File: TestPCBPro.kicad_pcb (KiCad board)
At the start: 2 copper layers, 100 x 50 mm, 82 parts, among them J1 Analog, J10 J3011G21DNL, J2 Digital, J3 CANBUS, J4 UART, J5 SPI, J6 I2C, J7 Power, J8 10118192-0001LF, J9 ICSP, SW1 Reset Button, U1 PIC32MX775F256L-80I/PT, U2 AZ1117EH-3.3TRG1, U3 LFSPXO025560REEL, U4 LAN8740A-EN, Y1 Crystal

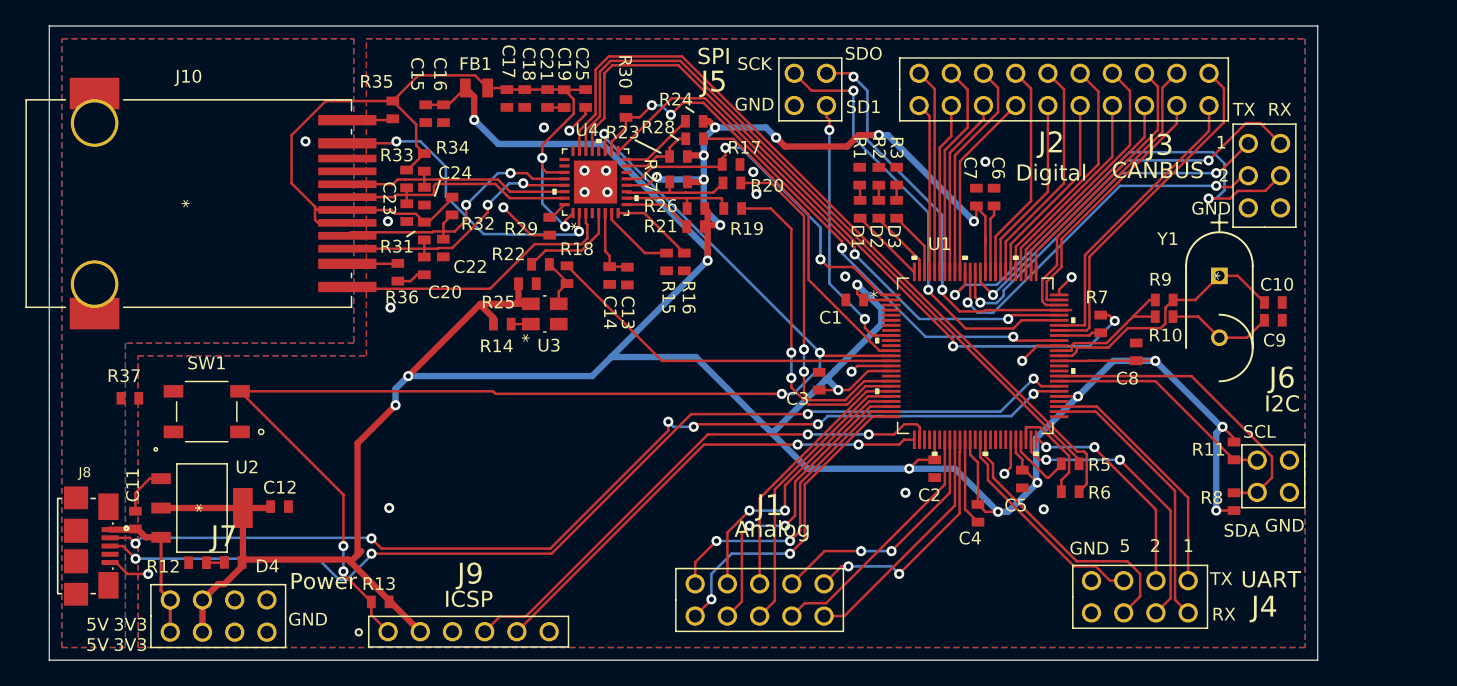
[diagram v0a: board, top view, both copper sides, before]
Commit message: Imported AISLER 2Layer-Complex design rules Added Silkscreen to all passives to help with orientation Moved C15 and C16 to the back in order to be physically closer to the VDDIO pin of the LAN8740a Increased trace width of some 5v traces to the proper 0.5mm
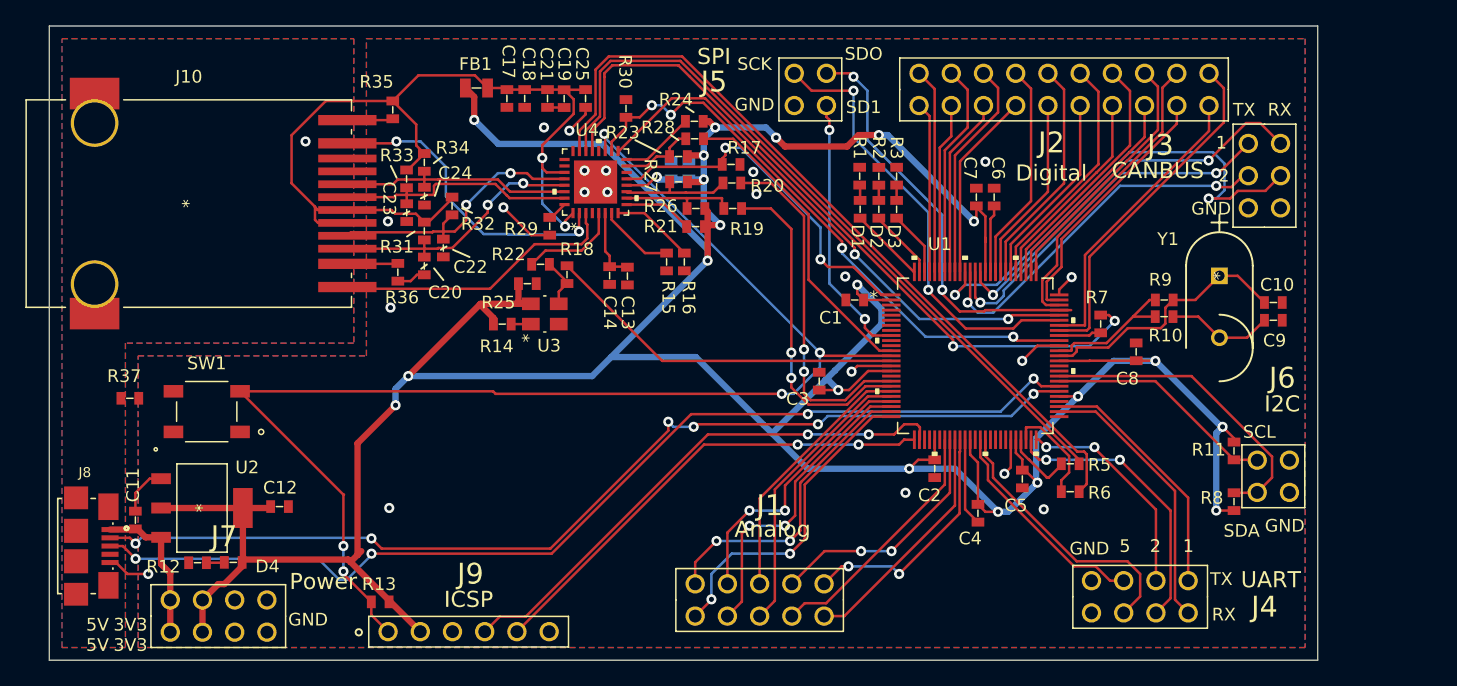
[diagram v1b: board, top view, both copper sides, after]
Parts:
- C14, C17, C21: value 1.0u -> 1u
- C15: value 1.0u -> 1u; moved to B.Cu
- C16: moved to B.Cu
- moved C15 21.8 mm to (132.8, 89.5), turned to 90 degrees
- moved C16 19.2 mm to (131.4, 89.5), turned to 90 degrees
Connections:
- net Net-(C13-Pad1) renamed /Ethernet/VDDCR
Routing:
- net +3V3: track 305.8 -> 302.2 mm

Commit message: Fixed nINT not actually being connected to 3v3 Changed the pic32MX7* 100 pin footprint from the T package to the F package Added some silkscreen around the DIGITAL and ANALOG headers
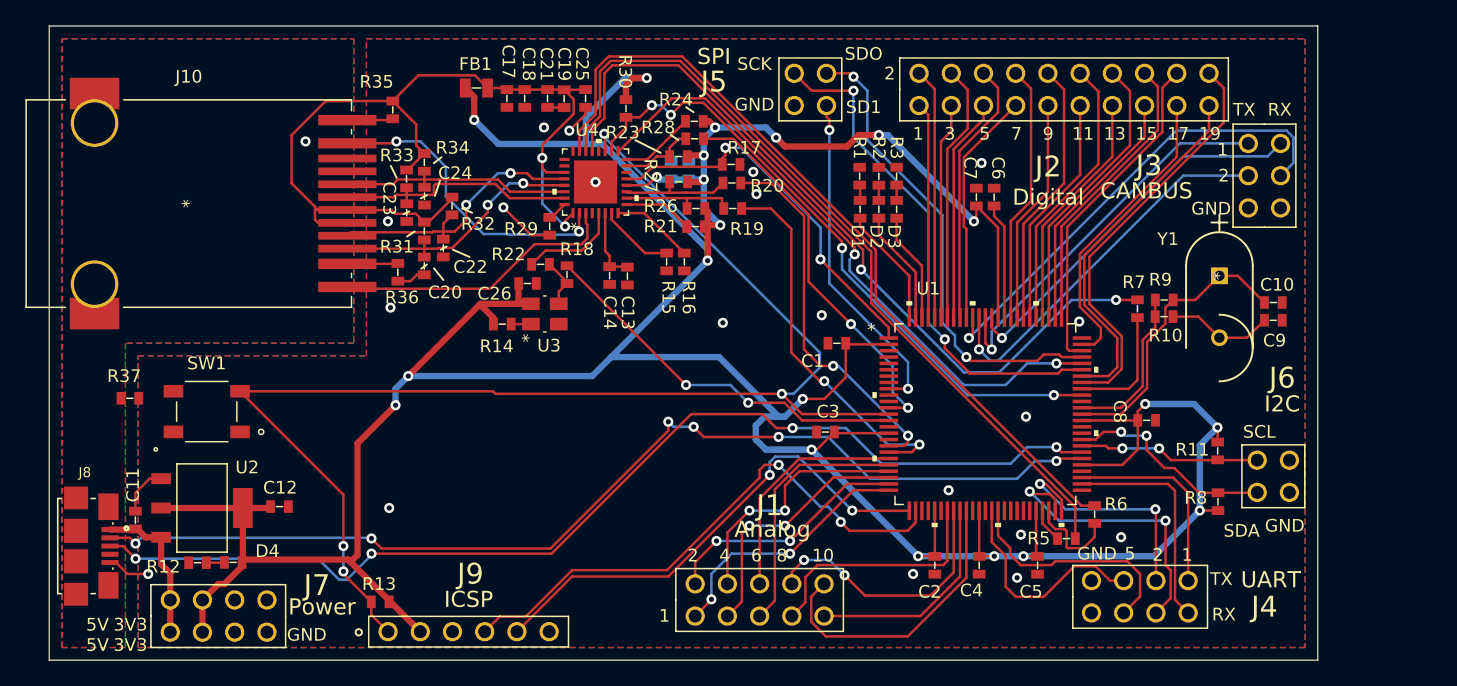
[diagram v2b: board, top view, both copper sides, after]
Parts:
- removed R25: 0.01u, Lambley:0603-1608M
- added C26: .01u, Lambley:0603-1608M, F.Cu at (119.5, 97.9)
- R15, R16, R17, R23, R26, R27: value 4.7K -> 4.7k
- U1: footprint ul_PIC32MX775F256L-80I-PT:PIC32MX775F256L-80I&slash_PT -> ul_PIC32MX764F128L-I-PF:PIC32MX764F128L-I&slash_PF
- moved C2 7.61 mm to (152.2, 118.4)
- moved C5 6.91 mm to (160.3, 118.4)
- moved R5 5.91 mm to (164.3, 116.8)
- moved C8 4.94 mm to (168.4, 108.7), turned to 0 degrees
- moved U1 4.67 mm to (156.8, 107.6)
- moved C4 4.10 mm to (155.7, 118.4)
- moved C1 3.69 mm to (146.2, 101.4)
- moved R7 3.14 mm to (169.4, 100.4)
- moved C3 2.49 mm to (145.3, 108.4), turned to 180 degrees
- moved R11 1.29 mm to (174.5, 109.3)
- moved R8 1.26 mm to (175.7, 115.7)
- moved R6 1.26 mm to (164.8, 114.4), turned to -90 degrees
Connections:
- R30 pad 1: +3.3V -> +3V3
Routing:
- net GND: track 36.2 -> 17.8 mm, vias 21 -> 20
- net +3V3: track 302.2 -> 314.5 mm
- net SDA2: track 24.6 -> 16.7 mm, vias 0 -> 2
- net Net-(R7-Pad1): track 3.36 -> 9.58 mm
- net /Ethernet/CRS_DV: track 24.8 -> 30.8 mm, vias 0 -> 2
- net /Ethernet/MDC: track 44.1 -> 50.0 mm
- net /Ethernet/TXD0: track 58.2 -> 64.0 mm
- net 69: track 23.4 -> 28.8 mm
- net 68: track 27.4 -> 32.8 mm
- net SDI1: track 21.1 -> 26.5 mm
- net AN0: track 25.7 -> 20.6 mm
- net AN1: track 24.6 -> 19.5 mm
- net SCK1: track 35.3 -> 40.3 mm
- net SDO1: track 33.0 -> 37.6 mm
- net /Ethernet/nINT: track 46.7 -> 51.0 mm
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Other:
- board text added: "10"
- board text added: "11"
- board text added: "13"
- board text added: "15"
- board text added: "17"
- board text added: "19"
- board text added: "3"
- board text added: "4"
- board text added: "6"
- board text added: "7"
- board text added: "8"
- board text added: "9"

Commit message: Added connection for MDIO to the PIC Complete redesign of board, reduced size from 100x50 to 75x35mm Readded C15 and C16 to the front Added some test points
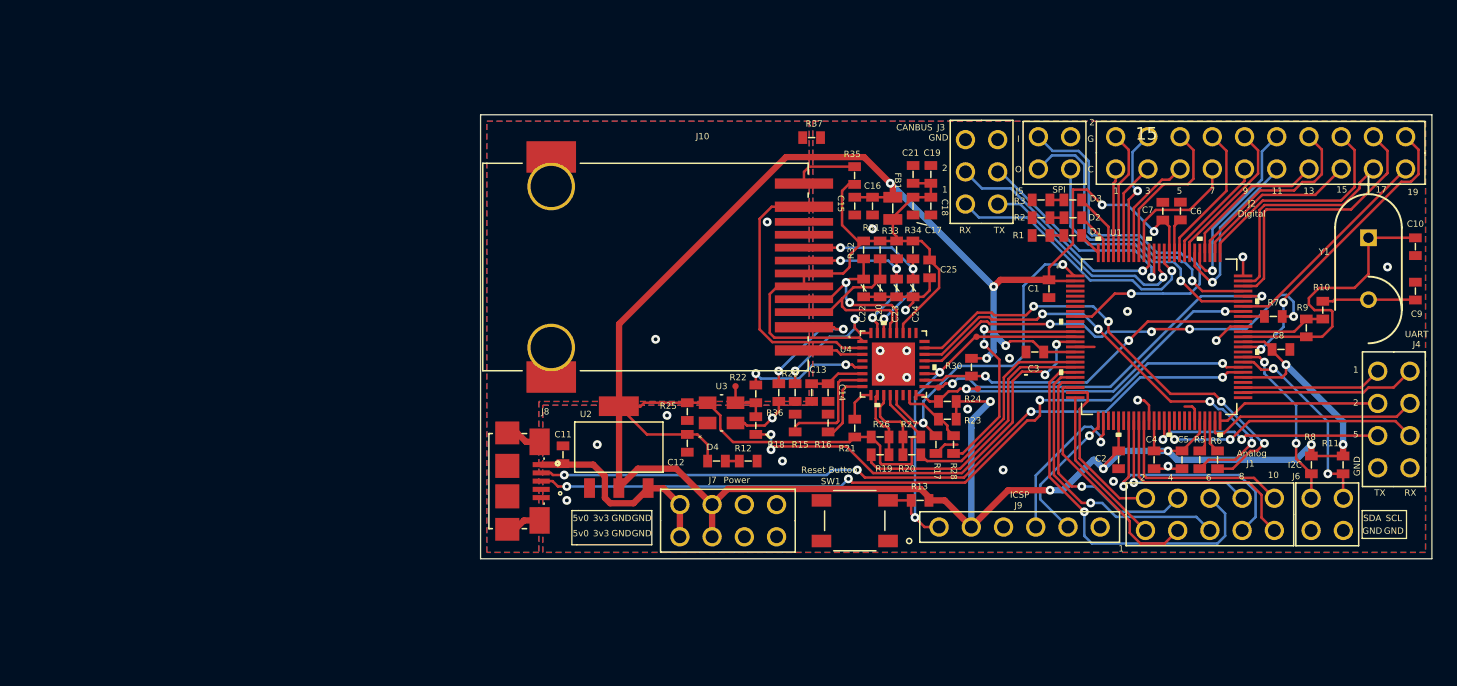
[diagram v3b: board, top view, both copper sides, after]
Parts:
- removed C26: .01u, Lambley:0603-1608M
- removed R14: 0-DNP, Lambley:0603-1608M
- added R25: 0.01u, Lambley:0603-1608M, F.Cu at (133.9, 108.5)
- added REF: .5mm TP, Lambley:.5mm TP, F.Cu at (153.1, 105.5)
- added REF**: .5mm TP, Lambley:.5mm TP, F.Cu at (156.1, 101.5)
- added REF**: .5mm TP, Lambley:.5mm TP, F.Cu at (137.1, 105.4)
- added REF**: .5mm TP, Lambley:.5mm TP, F.Cu at (156.2, 105.6)
- C15, C16: moved to F.Cu
- R15, R16, R17, R23, R26, R27: value 4.7k -> 4.7K
- U1: footprint ul_PIC32MX764F128L-I-PF:PIC32MX764F128L-I&slash_PF -> ul_PIC32MX775F256L-80I-PT:PIC32MX775F256L-80I&slash_PT
- moved R37 57.5 mm to (144.2, 85.2)
- moved SW1 51.8 mm to (146.5, 116.0)
- moved J9 44.2 mm to (153.2, 116.5)
- moved R13 43.3 mm to (150.5, 115.0)
- moved R12 41.7 mm to (136.9, 111.9), turned to 0 degrees
- moved D4 41.4 mm to (136.8, 110.7), turned to 180 degrees
- moved J7 40.9 mm to (132.7, 114.7)
- moved C24 39.2 mm to (150.5, 96.5)
- moved R34 39.1 mm to (151.7, 95.8)
- moved C23 39.1 mm to (149.2, 96.5)
- moved R33 39.0 mm to (150.4, 95.8)
- moved R35 38.3 mm to (147.1, 89.9), turned to 90 degrees
- moved J10 36.3 mm to (130.0, 96.0)
- moved J1 36.1 mm to (169.4, 114.2)
- moved C20 36.0 mm to (147.9, 96.5)
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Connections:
- net Net-(J10-Pad2) renamed /Ethernet/LED_LINK_OUT
- J2 pad 20: 68 -> 61
- R24 pad 2: Net-(R24-Pad2) -> /Ethernet/MDIO
- U1 pad 61: unconnected-(U1-Pad61) -> 61
- U1 pad 68: 68 -> /Ethernet/MDIO
- U3 pad 1: Net-(R14-Pad1) -> unconnected-(U3-Pad1)
- U4 pad 16: Net-(R24-Pad2) -> /Ethernet/MDIO
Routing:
- net /ICSP/MCLR: track 106.4 -> 30.9 mm, vias 4 -> 2
- net +3V3: track 314.5 -> 252.6 mm, vias 21 -> 13
- net 68: track 32.8 -> 0.00 mm
- net /Ethernet/MDIO: track 0.00 -> 30.0 mm, vias 0 -> 2
- net /ICSP/PGED: track 43.2 -> 13.3 mm, vias 2 -> 1
- net /ICSP/PGEC: track 39.0 -> 11.2 mm, vias 2 -> 1
- net /Ethernet/TX_EN: track 62.3 -> 34.5 mm, vias 2 -> 4
- net /Ethernet/TXD0: track 64.0 -> 36.7 mm, vias 0 -> 4
- net /Ethernet/TXD1: track 63.7 -> 37.8 mm, vias 0 -> 4
- net /USB and Power/D-: track 84.4 -> 59.3 mm, vias 6 -> 4
- net /USB and Power/D+: track 85.5 -> 60.6 mm
- net 61: track 0.00 -> 24.3 mm, vias 0 -> 2
- net /Ethernet/nINT: track 51.0 -> 27.4 mm, vias 4 -> 2
- net VDD1A: track 71.8 -> 48.9 mm, vias 2 -> 0
- net SCK1: track 40.3 -> 21.1 mm, vias 2 -> 1
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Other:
- board size 100 x 50 mm -> 75 x 35 mm
- board text added: "*"
- board text added: "3v3"
- board text added: "5v0"
- board text added: "C"
- board text added: "G"
- board text added: "I"
- board text added: "O"
- board text removed: "3V3"
- board text removed: "5V"
- board text removed: "SCK"
- board text removed: "SD1"
- board text removed: "SDO"

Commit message: Actually changed to the PIC to the F package this time
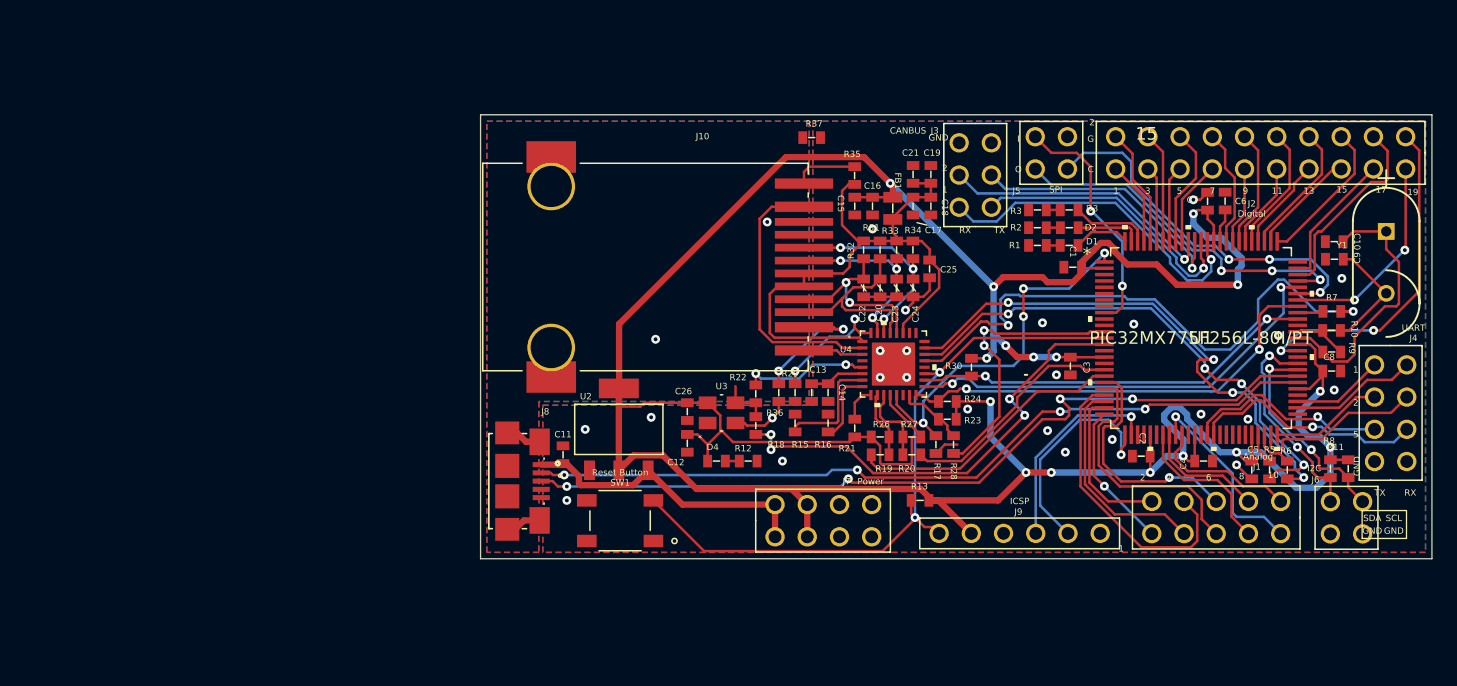
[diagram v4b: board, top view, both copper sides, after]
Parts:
- removed R25: 0.01u, Lambley:0603-1608M
- removed REF, REF** (x3): .5mm TP, Lambley:.5mm TP
- added C26: .01u, Lambley:0603-1608M, F.Cu at (132.7, 106.2)
- R15, R16, R17, R23, R26, R27: value 4.7K -> 4.7k
- U1: footprint ul_PIC32MX775F256L-80I-PT:PIC32MX775F256L-80I&slash_PT -> ul_PIC32MX764F128L-I-PF:PIC32MX764F128L-I&slash_PF
- moved SW1 18.5 mm to (128.0, 116.0)
- moved J7 7.50 mm to (140.2, 114.7)
- moved C9 7.23 mm to (185.5, 94.8), turned to 180 degrees
- moved R5 5.56 mm to (179.8, 113.2)
- moved R6 5.56 mm to (181.2, 113.2)
- moved C5 5.56 mm to (177.2, 110.8)
- moved C10 4.65 mm to (185.4, 93.4), turned to 180 degrees
- moved R7 4.63 mm to (183.0, 100.1)
- moved R9 4.48 mm to (185.2, 102.1), turned to 180 degrees
- moved C8 4.35 mm to (182.9, 104.8)
- moved C4 3.83 mm to (172.8, 111.9), turned to 0 degrees
- moved C1 3.80 mm to (164.8, 95.4), turned to 180 degrees
- moved C6 3.61 mm to (176.3, 92.0)
- moved C7 3.61 mm to (174.9, 92.0)
- moved C2 3.55 mm to (170.2, 110.3), turned to 180 degrees
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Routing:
- net /ICSP/MCLR: track 30.9 -> 54.7 mm
- net +3V3: track 252.6 -> 266.1 mm, vias 13 -> 16
- net SDI1: track 32.5 -> 19.0 mm, vias 1 -> 2
- net AN5: track 30.7 -> 19.0 mm
- net /Ethernet/TX_EN: track 34.5 -> 45.2 mm, vias 4 -> 2
- net GND: track 26.5 -> 17.5 mm, vias 21 -> 25
- net SCK1: track 21.1 -> 29.4 mm, vias 1 -> 3
- net AN8: track 20.4 -> 12.1 mm, vias 1 -> 0
- net 81: track 14.2 -> 6.73 mm, vias 1 -> 0
- net /ICSP/PGEC: track 11.2 -> 18.3 mm
- net +5V: track 16.7 -> 23.6 mm
- net 74: track 17.3 -> 10.9 mm
- net 76: track 17.6 -> 11.7 mm
- net 73: track 21.5 -> 15.6 mm
- net /Ethernet/MDIO: track 30.0 -> 35.2 mm
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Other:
- board text removed: "3v3"
- board text removed: "5v0"

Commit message: Re-added test points and fixed silkscreen
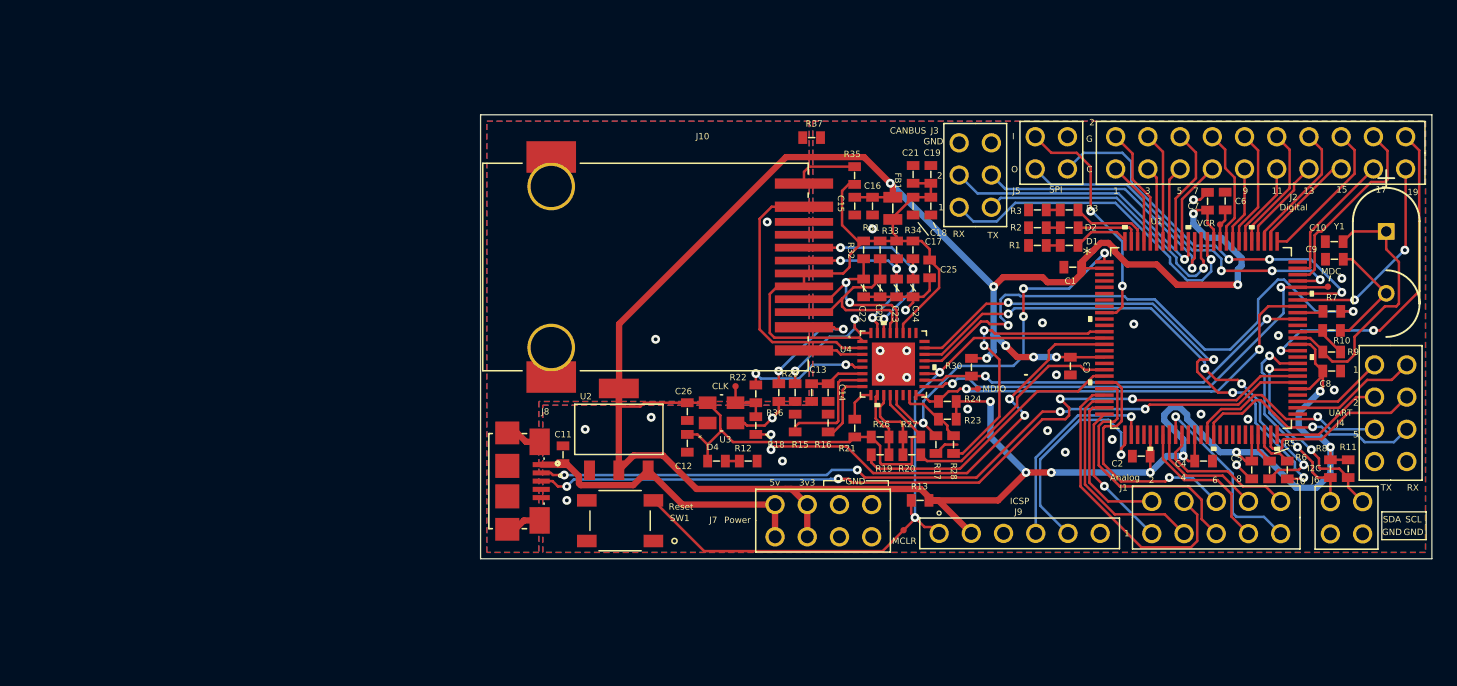
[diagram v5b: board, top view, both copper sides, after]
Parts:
- added CLK: .5mm TP, Lambley:.5mm TP, F.Cu at (137.1, 105.4)
- added MCLR: .5mm TP, Lambley:.5mm TP, F.Cu at (150.3, 116.8)
- added MDC: .5mm TP, Lambley:.5mm TP, F.Cu at (183.8, 97.5)
- added MDIO: .5mm TP, Lambley:.5mm TP, F.Cu at (156.2, 105.6)
- added VCR: .5mm TP, Lambley:.5mm TP, F.Cu at (175.3, 92.7)
- SW1: value Reset Button -> Reset
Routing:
- net /Ethernet/MDC: track 34.7 -> 37.1 mm
- net SCK1: track 29.4 -> 31.3 mm
- net /Ethernet/MDIO: track 35.2 -> 36.1 mm
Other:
- board text added: "3v3"
- board text added: "5v"
